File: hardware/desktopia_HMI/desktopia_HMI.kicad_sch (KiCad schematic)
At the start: 51 parts, among them J1 LCD_Connector, J2 RJ11 6P6C, J3 USB4105GFA, SW1 SW_Push, SW2 SW_Push, SW3 SW_Push, SW4 SW_Push, SW5 SW_Push, SW6 BOOT, U1 RP2040, U2 THVD1450D, U3 XC6206P332MR, U4 W25Q16JVSS, Y1 12MHz

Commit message: hardware: JLCPCB part numbers, safe TPS5430 enable, 24 V screw terminal, INA226 current sensor
- Every assembled part gets LCSC / jlcpcb PartNumber fields, Basic parts first (SP485EEN, SP3485EN,
  W25Q128JV, 12 MHz crystal with 33 pF, TS-1088 buttons, ...).
- TPS5430 ENA was tied to the 24 V input (7 V absolute maximum) and burnt the regulator: left open now.
- C25 10 uF 50 V ceramic input capacitor next to C2.
- 1.5 A barrel jack DC1 replaced by the 5.08 mm screw terminal J7.
- Analog CC6905 replaced by a 2 mOhm shunt + INA226 on I2C (0x40), alert on PE6; PF0 is free.

Co-Authored-By: Claude Opus 5.5 <noreply@anthropic.com>
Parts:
- removed J3: USB4105GFA, JLCImport:GCT_USB4105GFA, symbol USB4105GFA:USB4105GFA
- removed U2: THVD1450D, Package_SO:SOIC-8_3.9x4.9mm_P1.27mm, symbol Interface_UART:THVD1450D
- removed U4: W25Q16JVSS, Package_SO:SOIC-8_5.3x5.3mm_P1.27mm, symbol Memory_Flash:W25Q16JVSS
- added J3: TYPE-C-31-M-12, Connector_USB:USB_C_Receptacle_HRO_TYPE-C-31-M-12, symbol Connector:USB_C_Receptacle_USB2.0_16P
- added U2: SP3485EN-L/TR, Package_SO:SOIC-8_3.9x4.9mm_P1.27mm, symbol Interface_UART:SP3485EN
- added U4: W25Q128JVSIQ, Package_SO:SOIC-8_5.3x5.3mm_P1.27mm, symbol Memory_Flash:W25Q128JVS
- C1, C10, C11, C12, C13, C15, C17, C18, C6, C7, C8, C9: LCSC (none) -> C1525
- C14, C16, C3, C4: LCSC (none) -> C52923
- C19, C20: value 15pF -> 33pF; LCSC (none) -> C1562; jlcpcb PartNumber (none) -> C1562
- C2: LCSC (none) -> C19702; jlcpcb PartNumber (none) -> C19702
- D1: LCSC (none) -> C2480
- J2: LCSC (none) -> C3097716; jlcpcb PartNumber (none) -> C3097716
- R1: LCSC (none) -> C25079; jlcpcb PartNumber (none) -> C25079
- R2, R3: LCSC (none) -> C25905
- R4, R5: value 27 -> 22; LCSC (none) -> C25092; jlcpcb PartNumber (none) -> C25092
- R6, R8: LCSC (none) -> C11702; jlcpcb PartNumber (none) -> C11702
- R7: LCSC (none) -> C25744
- SW1, SW2, SW3, SW4, SW5: LCSC (none) -> C5333465; jlcpcb PartNumber (none) -> C5333465
- SW6: value BOOT -> TS-1088-AR02016; footprint JLCImport:DTS41 -> Button_Switch_SMD:SW_SPST_TS-1088-xR020; LCSC (none) -> C720477; jlcpcb PartNumber (none) -> C720477
- U1: LCSC (none) -> C2040; jlcpcb PartNumber (none) -> C2040
- U3: LCSC (none) -> C5446; jlcpcb PartNumber (none) -> C5446
- Y1: LCSC (none) -> C9002; jlcpcb PartNumber (none) -> C9002
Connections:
- net +3V3: now also U2.8 (VCC), U4.8 (VCC)
- net CC1: now also J3.A5 (CC1)
- net CC2: now also J3.B5 (CC2)
- net GND: now also J3.A1 (GND), J3.A12 (GND), J3.B1 (GND), J3.B12 (GND), J3.SH (SHIELD), U2.5 (GND), U4.4 (GND)
- net LINK_DE: now also U2.2 (~{RE}), U2.3 (DE)
- net LINK_RX: now also U2.1 (RO)
- net LINK_TX: now also U2.4 (DI)
- net QSPI_SCLK: now also U4.6 (CLK)
- net QSPI_SD0: now also U4.5 (DI/IO_{0})
- net QSPI_SD1: now also U4.2 (DO/IO_{1})
- net QSPI_SD2: now also U4.3 (~{WP}/IO_{2})
- net QSPI_SD3: now also U4.7 (~{HOLD}/~{RESET}/IO_{3})
- net QSPI_SS: now also U4.1 (~{CS})
- net RS485_A: now also U2.6 (A)
- net RS485_B: now also U2.7 (B)
- net at R5.1: now also J3.A7 (D-), J3.B7 (D-)
- net at R4.1: now also J3.A6 (D+), J3.B6 (D+)
- net VBUS: no longer names the net of D1.2 (A)
- net VBUS: now also J3.A4 (VBUS), J3.A9 (VBUS), J3.B4 (VBUS), J3.B9 (VBUS)

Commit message: hardware: HMI cord soldered to the board instead of an RJ11 jack
The HMI board sits at 45 deg under the desk edge: a jack would stand 12 mm off the board and send the
cord off at 45 deg to the desk. J2 is now Desktopia:Cable_6P6C_SolderPads (6 pads at 2.54 mm, cable-tie
strain relief, board-edge mark), generated by kicad_library/pcb/tools/cable_6p6c_fp.py. The RJ11 plug
stays on the motherboard end. Also includes the reorganised HMI schematic layout.

Co-Authored-By: Claude Opus 5.5 <noreply@anthropic.com>
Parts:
- J2: value RJ11 6P6C -> 6P6C cord, soldered; footprint Connector_RJ:RJ12_Amphenol_54601-x06_Horizontal -> Desktopia:Cable_6P6C_SolderPads; LCSC C3097716 -> (none); jlcpcb PartNumber C3097716 -> (none); now left out of the parts list
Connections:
- net +5V: now also J1.7 (Pin_7); no longer J1.1 (Pin_1)
- net GND: now also J1.6 (Pin_6); no longer J1.2 (Pin_2)
- net LCD_CS: now also J1.2 (Pin_2); no longer J1.6 (Pin_6)
- net LCD_DC: now also J1.3 (Pin_3); no longer J1.5 (Pin_5)
- net LCD_RST: now also J1.1 (Pin_1); no longer J1.7 (Pin_7)
- net LCD_SCK: now also J1.5 (Pin_5); no longer J1.3 (Pin_3)
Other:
- note added: "7 = +5V (VCC) 6 = GND"
- note added: "Cord: 6 conductors (6P6C), straight or reversed. 1 = +5V 2 = GND 3 = A 4 = B 5 = GND 6 = +5V Symmetric: a reversed telephone cord cannot swap +5V and GND, it only swaps A and B - the firmware detects it and inverts the UART pads (gpio_set_inover / outover). J2: the cord is soldered to the board (no jack: the board sits at 45 deg under the desk edge, the cord leaves flat along the desk). Keep the 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"
- note removed: "1 = +5V (VCC) 2 = GND"
- note removed: "Cord: 6 conductors (6P6C), straight or reversed. 1 = +5V 2 = GND 3 = A 4 = B 5 = GND 6 = +5V Symmetric: a reversed telephone cord cannot swap +5V and GND, it only swaps A and B - the firmware detects it and inverts the UART pads (gpio_set_inover / outover)."

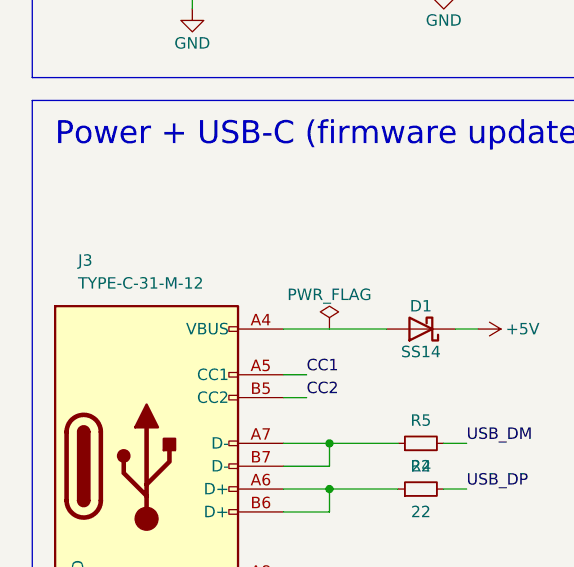
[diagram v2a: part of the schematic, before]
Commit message: hardware: JLCPCB cost pass, motor input with margin, BSS138 level shifters
Motherboard:
- Extended part numbers 12 -> 9: TXS0104E -> BSS138 level shifters (Preferred),
  C4 electrolytic -> 2 x 47 uF ceramic with the TI SLVA237 compensation,
  J5 -> the same KF128 terminal as J4 / J7, J3 GCT USB4105 (out of stock)
  -> G-Switch GT-USB-7010ASV, R1 + R2 -> R1, F1 -> 30 V PTC.
- 24 V input with margin: SMBJ28A TVS, 220 uF 50 V bulk, 24 A terminals.
  5 V rail good for 1.5 A: 22 uH 1.8 A inductor, SS34.
- Sensor rail stays at 2.8 V (VL53L1CB typical, 0.7 V under its maximum).
  VL53L1CB GPIO1 -> TOF_INT on PB4 (PCINT4) through a third BSS138.
- 10k pull-downs on Mpwm / Mdir. INA226 alert kept on INT6, with a 4.7k
  pull-up and a 100 pF filter.

HMI: USB-C G-Switch GT-USB-7010ASV ($0.09 instead of $0.19).

READMEs and the firmware pin comments follow the schematics.

Co-Authored-By: Claude Opus 5.5 <noreply@anthropic.com>
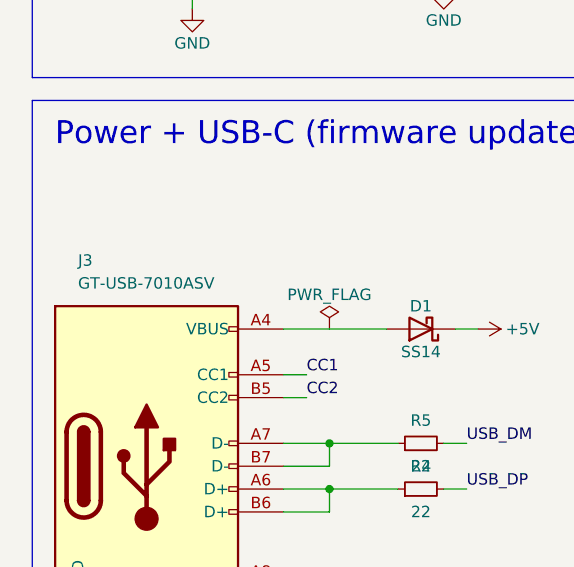
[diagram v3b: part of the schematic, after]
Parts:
- J3: value TYPE-C-31-M-12 -> GT-USB-7010ASV; footprint Connector_USB:USB_C_Receptacle_HRO_TYPE-C-31-M-12 -> Connector_USB:USB_C_Receptacle_G-Switch_GT-USB-7010ASV; LCSC C165948 -> C2988369; jlcpcb PartNumber C165948 -> C2988369
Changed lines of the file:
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@@
 			)
 		)
-		(property "Value" "TYPE-C-31-M-12"
+		(property "Value" "GT-USB-7010ASV"
 			(at 17.78 127 0)
 			(show_name no)
@@
 			)
 		)
-		(property "Footprint" "Connector_USB:USB_C_Receptacle_HRO_TYPE-C-31-M-12"
+		(property "Footprint" "Connector_USB:USB_C_Receptacle_G-Switch_GT-USB-7010ASV"
 			(at 25.4 147.32 0)
 			(hide yes)
@@
 			)
 		)
-		(property "Datasheet" ""
+		(property "Datasheet" "https://datasheet.lcsc.com/lcsc/2204071530_G-Switch-GT-USB-7010ASV_C2988369.pdf"
 			(at 25.4 147.32 0)
 			(hide yes)
@@
 			)
 		)
-		(property "Description" "USB 2.0-only 16P Type-C Receptacle"
+		(property "Description" "USB 2.0 Type-C receptacle, 16 pins, SMD, right angle"
 			(at 25.4 147.32 0)
 			(hide yes)
@@
 			)
 		)
-		(property "LCSC" "C165948"
+		(property "LCSC" "C2988369"
 			(at 25.4 147.32 0)
 			(hide yes)
@@
 			)
 		)
-		(property "jlcpcb PartNumber" "C165948"
+		(property "jlcpcb PartNumber" "C2988369"
 			(at 25.4 147.32 0)
 			(hide yes)

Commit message: hardware: motor supply switch, schematics redrawn with fewer labels, re-annotation
Motherboard:
- Q5 P-MOSFET high-side switch on the driver supply (Q4 gate driver, D3 clamp,
  C21 soft start, R22 pull-down), driven by PD7 (MOTOR_PWR); TP13 on MOTOR_SW
- Schematic redrawn: wires instead of labels inside each block (76 -> 22 labels),
  same netlist
- J6 motor command terminal: 3 pins again (ZX-DG28L-2.54-3P), pin 3 = driver logic GND
- C6 24 V bulk: 220 uF 10 x 10 mm -> 100 uF 8 x 10 mm (C970687), same cable damping
- Re-annotated; TP9 on TOF_INT, H3 mounting hole, J3 and Y1 symbols updated,
  HWB left open; notes and README follow the new references

HMI board:
- Schematic redrawn without labels (70 -> 0), same netlist

The PCB files are not part of this commit.

Co-Authored-By: Claude Opus 5.5 <noreply@anthropic.com>
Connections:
- net BTN_DOWN: no longer names the net of SW2.1, U1.15 (GPIO12)
- net BTN_PRESET1: no longer names the net of SW3.1, U1.16 (GPIO13)
- net BTN_PRESET2: no longer names the net of SW4.1, U1.17 (GPIO14)
- net BTN_PRESET3: no longer names the net of SW5.1, U1.18 (GPIO15)
- net BTN_UP: no longer names the net of SW1.1, U1.14 (GPIO11)
- net CC1: no longer names the net of J3.A5 (CC1), R2.1
- net CC2: no longer names the net of J3.B5 (CC2), R3.1
- net LCD_CS: no longer names the net of J1.2 (Pin_2), TP5.1, U1.28 (GPIO17)
- net LCD_DC: no longer names the net of J1.3 (Pin_3), TP4.1, U1.31 (GPIO20)
- net LCD_MOSI: no longer names the net of J1.4 (Pin_4), TP3.1, U1.30 (GPIO19)
- net LCD_RST: no longer names the net of J1.1 (Pin_1), TP6.1, U1.32 (GPIO21)
- net LCD_SCK: no longer names the net of J1.5 (Pin_5), TP2.1, U1.29 (GPIO18)
- net LINK_DE: no longer names the net of U1.4 (GPIO2), U2.2 (~{RE}), U2.3 (DE)
- net LINK_RX: no longer names the net of U1.3 (GPIO1), U2.1 (RO)
- net LINK_TX: no longer names the net of U1.2 (GPIO0), U2.4 (DI)
- net QSPI_SCLK: no longer names the net of U1.52 (QSPI_SCLK), U4.6 (CLK)
- net QSPI_SD0: no longer names the net of U1.53 (QSPI_SD0), U4.5 (DI/IO_{0})
- net QSPI_SD1: no longer names the net of U1.55 (QSPI_SD1), U4.2 (DO/IO_{1})
- net QSPI_SD2: no longer names the net of U1.54 (QSPI_SD2), U4.3 (~{WP}/IO_{2})
- net QSPI_SD3: no longer names the net of U1.51 (QSPI_SD3), U4.7 (~{HOLD}/~{RESET}/IO_{3})
- net QSPI_SS: no longer names the net of R6.1, U1.56 (~{QSPI_SS}), U4.1 (~{CS})
- net RS485_A: no longer names the net of J2.3, R1.1, U2.6 (A)
- net RS485_B: no longer names the net of J2.4, R1.2, U2.7 (B)
- net RUN: no longer names the net of R7.2, TP9.1, U1.26 (RUN)
- net SWCLK: no longer names the net of TP7.1, U1.24 (SWCLK)
- net SWDIO: no longer names the net of TP8.1, U1.25 (SWDIO)
- net USB_DM: no longer names the net of R5.2, U1.46 (USB_DM)
- net USB_DP: no longer names the net of R4.2, U1.47 (USB_DP)
- net XIN: no longer names the net of C19.1, U1.20 (XIN), Y1.1
- net XOUT: no longer names the net of R8.2, U1.21 (XOUT)
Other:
- note added: "J1: 7 = +5V (VCC) 6 = GND"
- note added: "J2: 1, 6 = +5V 2, 5 = GND (power symbols at the pins)"
- note added: "SWD: TP7 SWCLK, TP8 SWDIO, TP10 GND, TP9 RUN"
- note removed: "7 = +5V (VCC) 6 = GND"
- note removed: "SWD"
- moved on the sheet: C1, C10, C11, C12, C13, C14, C15, C16, C17, C18, C19, C2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

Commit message: hardware: HMI board re-annotated, PCB updated from the RP2040 schematic
The PCB now holds the RP2040 design (references included); the routing is not finished. README tables, connector pin-outs, test points and assembly notes follow the new references.

Co-Authored-By: Claude Opus 5.5 <noreply@anthropic.com>
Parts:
- renumbered C2 to C1, C20 to C10, C1 to C19, C3 to C2, C4 to C3, C6 to C4, C7 to C5, C8 to C6, C9 to C7, C19 to C8, C10 to C9, J3 to J1, J1 to J2, J2 to J3, R2 to R1, R5 to R2, R6 to R5, R8 to R6, R1 to R8, SW6 to SW1, SW1 to SW2, SW2 to SW3, SW3 to SW4, SW4 to SW5, SW5 to SW6, TP10 to TP1, TP9 to TP2, TP8 to TP3, TP7 to TP4, TP2 to TP5, TP3 to TP6, TP4 to TP7, TP5 to TP8, TP6 to TP9, U3 to U1, U4 to U2, U1 to U3, U2 to U4
